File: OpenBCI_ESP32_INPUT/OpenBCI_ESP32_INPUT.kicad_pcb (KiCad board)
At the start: 2 copper layers, 50 x 50 mm, 75 parts, among them J1 Conn_02x13_Odd_Even, J2 Conn_02x08_Odd_Even, J3 Conn_02x03_Odd_Even, J4 Conn_02x02_Odd_Even, U1 TPD4E1B06, U2 TPD4E1B06, U3 TPD4E1B06, U4 TPD4E1B06, U5 TPD4E1B06, U6 TPD4E1B06, U7 ADS1299IPAG1

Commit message: Update Input Board Silk Screen
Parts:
- added R25: 0R, Resistor_SMD:R_0603_1608Metric, F.Cu at (124.6, 61.7)
- added R26: 0R, Resistor_SMD:R_0603_1608Metric, F.Cu at (119.8, 60.0)
- added R27: 0R, Resistor_SMD:R_0603_1608Metric, F.Cu at (124.6, 60.0)
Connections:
- C24 pad 2: /ADS1299/IBIAS -> Net-(C24-Pad2)
- R17 pad 2: /ADS1299/IBIAS -> Net-(C24-Pad2)
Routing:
- net Net-(C24-Pad2): track 0.00 -> 7.94 mm
- net Net-(C24-Pad1): track 8.88 -> 10.6 mm
- net /ADS1299/BIAS_INV: track 21.9 -> 22.9 mm

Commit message: Latest PCB file and firmware
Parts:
- added R28: 0R, Resistor_SMD:R_0603_1608Metric, F.Cu at (144.2, 63.8)
- added R29: 0R, Resistor_SMD:R_0603_1608Metric, F.Cu at (144.2, 65.5)
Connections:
- J2 pad 13: Net-(J2-Pad13) -> unconnected-(J2-Pad13)
- J2 pad 5: Net-(J2-Pad5) -> unconnected-(J2-Pad5)
- J2 pad 7: Net-(J2-Pad7) -> unconnected-(J2-Pad7)
- U1 pad 4: Net-(U1-Pad4) -> unconnected-(U1-Pad4)
- U6 pad 4: Net-(U6-Pad4) -> unconnected-(U6-Pad4)
- U6 pad 5: Net-(U6-Pad5) -> unconnected-(U6-Pad5)
- U7 pad 27: Net-(U7-Pad27) -> unconnected-(U7-Pad27)
- U7 pad 29: Net-(U7-Pad29) -> unconnected-(U7-Pad29)
- U7 pad 38: Net-(U7-Pad38) -> unconnected-(U7-Pad38)
- U7 pad 42: Net-(U7-Pad42) -> unconnected-(U7-Pad42)
- U7 pad 44: Net-(U7-Pad44) -> unconnected-(U7-Pad44)
- U7 pad 45: Net-(U7-Pad45) -> unconnected-(U7-Pad45)
- U7 pad 46: Net-(U7-Pad46) -> unconnected-(U7-Pad46)
- U7 pad 52: +3V3 -> Net-(U7-Pad52)
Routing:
- net Net-(U7-Pad52): track 0.00 -> 17.5 mm, vias 0 -> 2
- net GND: track 51.7 -> 56.1 mm
- net +2V5: track 75.7 -> 73.2 mm, vias 4 -> 3
- net -2V5: track 103.9 -> 102.6 mm
- net /ADS1299/CS: track 8.00 -> 7.19 mm
- added copper zone on F.Cu, net GND
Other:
- net class Default removed

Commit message: Code and STL updates
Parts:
- R28: value 0R -> NF
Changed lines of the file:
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@@
   (net 31 "unconnected-(J2-Pad7)")
   (net 32 "unconnected-(J2-Pad13)")
-  (net 33 "Net-(U7-Pad52)")
+  (net 33 "Net-(R28-Pad2)")
   (net 34 "unconnected-(U1-Pad4)")
   (net 35 "unconnected-(U6-Pad4)")
@@
       (net 2 "-2V5") (pinfunction "AVSS") (pintype "power_in"))
     (pad "21" smd roundrect locked (at -1.75 5.6625) (size 0.3 1.475) (layers "F.Cu" "F.Paste" "F.Mask") (roundrect_rratio 0.25)
-      (net 10 "+2V5") (pinfunction "AVDD") (pintype "passive"))
+      (net 10 "+2V5") (pinfunction "AVDD") (pintype "power_in"))
     (pad "22" smd roundrect locked (at -1.25 5.6625) (size 0.3 1.475) (layers "F.Cu" "F.Paste" "F.Mask") (roundrect_rratio 0.25)
-      (net 10 "+2V5") (pinfunction "AVDD") (pintype "passive"))
+      (net 10 "+2V5") (pinfunction "AVDD") (pintype "power_in"))
     (pad "23" smd roundrect locked (at -0.75 5.6625) (size 0.3 1.475) (layers "F.Cu" "F.Paste" "F.Mask") (roundrect_rratio 0.25)
-      (net 2 "-2V5") (pinfunction "AVSS") (pintype "passive"))
+      (net 2 "-2V5") (pinfunction "AVSS") (pintype "power_in"))
     (pad "24" smd roundrect locked (at -0.25 5.6625) (size 0.3 1.475) (layers "F.Cu" "F.Paste" "F.Mask") (roundrect_rratio 0.25)
       (net 7 "/ADS1299/VREF") (pinfunction "VREFP") (pintype "passive"))
@@
       (net 1 "GND") (pinfunction "RESV1") (pintype "input"))
     (pad "32" smd roundrect locked (at 3.75 5.6625) (size 0.3 1.475) (layers "F.Cu" "F.Paste" "F.Mask") (roundrect_rratio 0.25)
-      (net 2 "-2V5") (pinfunction "AVSS") (pintype "passive"))
+      (net 2 "-2V5") (pinfunction "AVSS") (pintype "power_in"))
     (pad "33" smd roundrect locked (at 5.6625 3.75) (size 1.475 0.3) (layers "F.Cu" "F.Paste" "F.Mask") (roundrect_rratio 0.25)
       (net 1 "GND") (pinfunction "DGND") (pintype "power_in"))
@@
       (net 9 "+3V3") (pinfunction "DVDD") (pintype "power_in"))
     (pad "49" smd roundrect locked (at 3.75 -5.6625) (size 0.3 1.475) (layers "F.Cu" "F.Paste" "F.Mask") (roundrect_rratio 0.25)
-      (net 1 "GND") (pinfunction "DGND") (pintype "passive"))
+      (net 1 "GND") (pinfunction "DGND") (pintype "power_in"))
     (pad "50" smd roundrect locked (at 3.25 -5.6625) (size 0.3 1.475) (layers "F.Cu" "F.Paste" "F.Mask") (roundrect_rratio 0.25)
-      (net 9 "+3V3") (pinfunction "DVDD") (pintype "passive"))
+      (net 9 "+3V3") (pinfunction "DVDD") (pintype "power_in"))
     (pad "51" smd roundrect locked (at 2.75 -5.6625) (size 0.3 1.475) (layers "F.Cu" "F.Paste" "F.Mask") (roundrect_rratio 0.25)
-      (net 1 "GND") (pinfunction "DGND") (pintype "passive"))
+      (net 1 "GND") (pinfunction "DGND") (pintype "power_in"))
     (pad "52" smd roundrect locked (at 2.25 -5.6625) (size 0.3 1.475) (layers "F.Cu" "F.Paste" "F.Mask") (roundrect_rratio 0.25)
-      (net 33 "Net-(U7-Pad52)") (pinfunction "CLKSEL") (pintype "input"))
+      (net 33 "Net-(R28-Pad2)") (pinfunction "CLKSEL") (pintype "input"))
     (pad "53" smd roundrect locked (at 1.75 -5.6625) (size 0.3 1.475) (layers "F.Cu" "F.Paste" "F.Mask") (roundrect_rratio 0.25)
       (net 2 "-2V5") (pinfunction "AVSS1") (pintype "power_in"))
@@
       (net 5 "Net-(C19-Pad1)") (pinfunction "VCAP3") (pintype "passive"))
     (pad "56" smd roundrect locked (at 0.25 -5.6625) (size 0.3 1.475) (layers "F.Cu" "F.Paste" "F.Mask") (roundrect_rratio 0.25)
-      (net 10 "+2V5") (pinfunction "AVDD") (pintype "passive"))
+      (net 10 "+2V5") (pinfunction "AVDD") (pintype "power_in"))
     (pad "57" smd roundrect locked (at -0.25 -5.6625) (size 0.3 1.475) (layers "F.Cu" "F.Paste" "F.Mask") (roundrect_rratio 0.25)
-      (net 2 "-2V5") (pinfunction "AVSS") (pintype "passive"))
+      (net 2 "-2V5") (pinfunction "AVSS") (pintype "power_in"))
     (pad "58" smd roundrect locked (at -0.75 -5.6625) (size 0.3 1.475) (layers "F.Cu" "F.Paste" "F.Mask") (roundrect_rratio 0.25)
-      (net 2 "-2V5") (pinfunction "AVSS") (pintype "passive"))
+      (net 2 "-2V5") (pinfunction "AVSS") (pintype "power_in"))
     (pad "59" smd roundrect locked (at -1.25 -5.6625) (size 0.3 1.475) (layers "F.Cu" "F.Paste" "F.Mask") (roundrect_rratio 0.25)
-      (net 10 "+2V5") (pinfunction "AVDD") (pintype "passive"))
+      (net 10 "+2V5") (pinfunction "AVDD") (pintype "power_in"))
     (pad "60" smd roundrect locked (at -1.75 -5.6625) (size 0.3 1.475) (layers "F.Cu" "F.Paste" "F.Mask") (roundrect_rratio 0.25)
       (net 1 "GND") (pinfunction "BIASREF") (pintype "input"))
@@
       (net 8 "Net-(C24-Pad1)") (pinfunction "BIASOUT") (pintype "output"))
     (pad "64" smd roundrect locked (at -3.75 -5.6625) (size 0.3 1.475) (layers "F.Cu" "F.Paste" "F.Mask") (roundrect_rratio 0.25)
-      (net 1 "GND") (pinfunction "RSRVD") (pintype "output"))
+      (net 1 "GND") (pinfunction "RSRVD") (pintype "input"))
     (model "${KICAD6_3DMODEL_DIR}/Package_QFP.3dshapes/TQFP-64_10x10mm_P0.5mm.wrl"
       (offset (xyz 0 0 0))
@@
     (fp_line (start -0.8 0.4125) (end -0.8 -0.4125) (layer "F.Fab") (width 0.1))
     (pad "1" smd roundrect locked (at -0.825 0) (size 0.8 0.95) (layers "F.Cu" "F.Paste" "F.Mask") (roundrect_rratio 0.25)
-      (net 33 "Net-(U7-Pad52)") (pintype "passive"))
+      (net 33 "Net-(R28-Pad2)") (pintype "passive"))
     (pad "2" smd roundrect locked (at 0.825 0) (size 0.8 0.95) (layers "F.Cu" "F.Paste" "F.Mask") (roundrect_rratio 0.25)
       (net 9 "+3V3") (pintype "passive"))
@@
       (effects (font (size 0.8 0.8) (thickness 0.1)))
     )
-    (fp_text value "0R" (at 0 1.43) (layer "F.Fab")
+    (fp_text value "NF" (at 0 1.43) (layer "F.Fab")
       (effects (font (size 1 1) (thickness 0.15)))
     )
@@
       (net 1 "GND") (pintype "passive"))
     (pad "2" smd roundrect locked (at 0.825 0) (size 0.8 0.95) (layers "F.Cu" "F.Paste" "F.Mask") (roundrect_rratio 0.25)
-      (net 33 "Net-(U7-Pad52)") (pintype "passive"))
+      (net 33 "Net-(R28-Pad2)") (pintype "passive"))
     (model "${KICAD6_3DMODEL_DIR}/Resistor_SMD.3dshapes/R_0603_1608Metric.wrl" hide
       (offset (xyz 0 0 0))

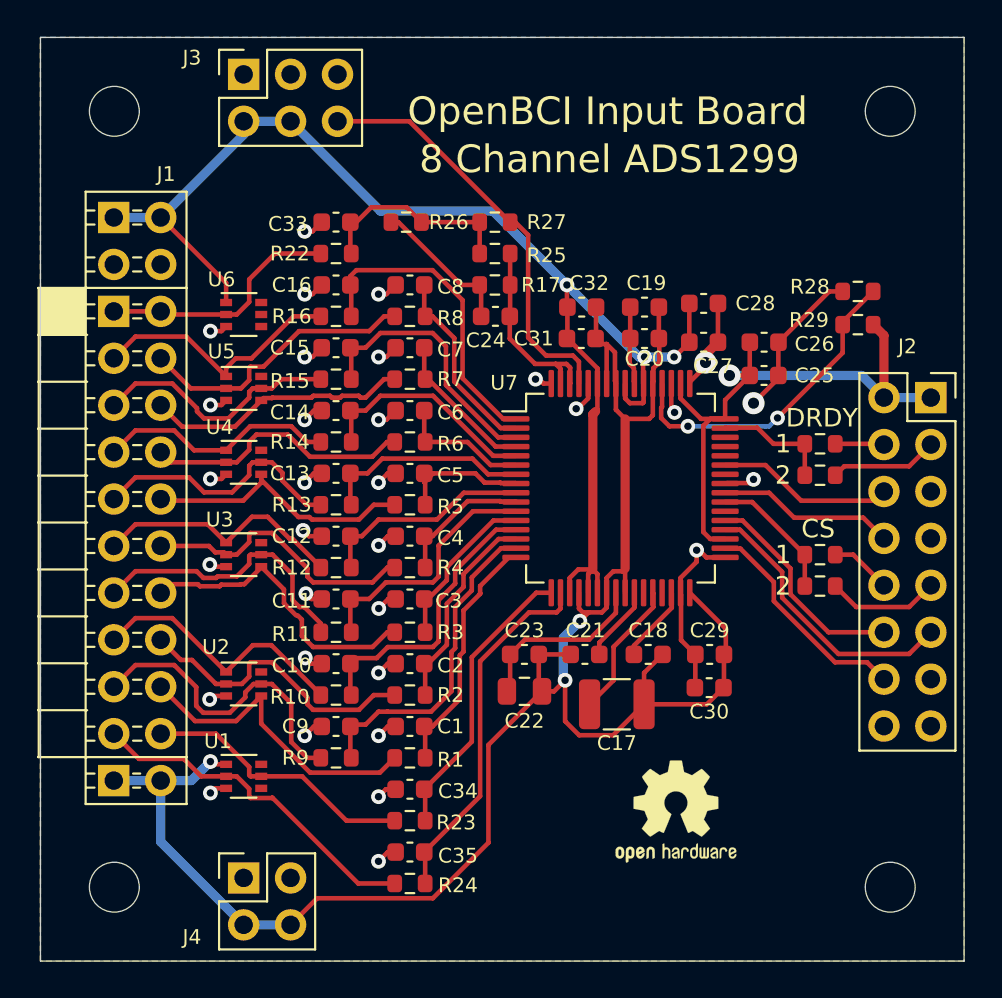
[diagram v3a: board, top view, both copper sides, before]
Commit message: add ADS1298 files
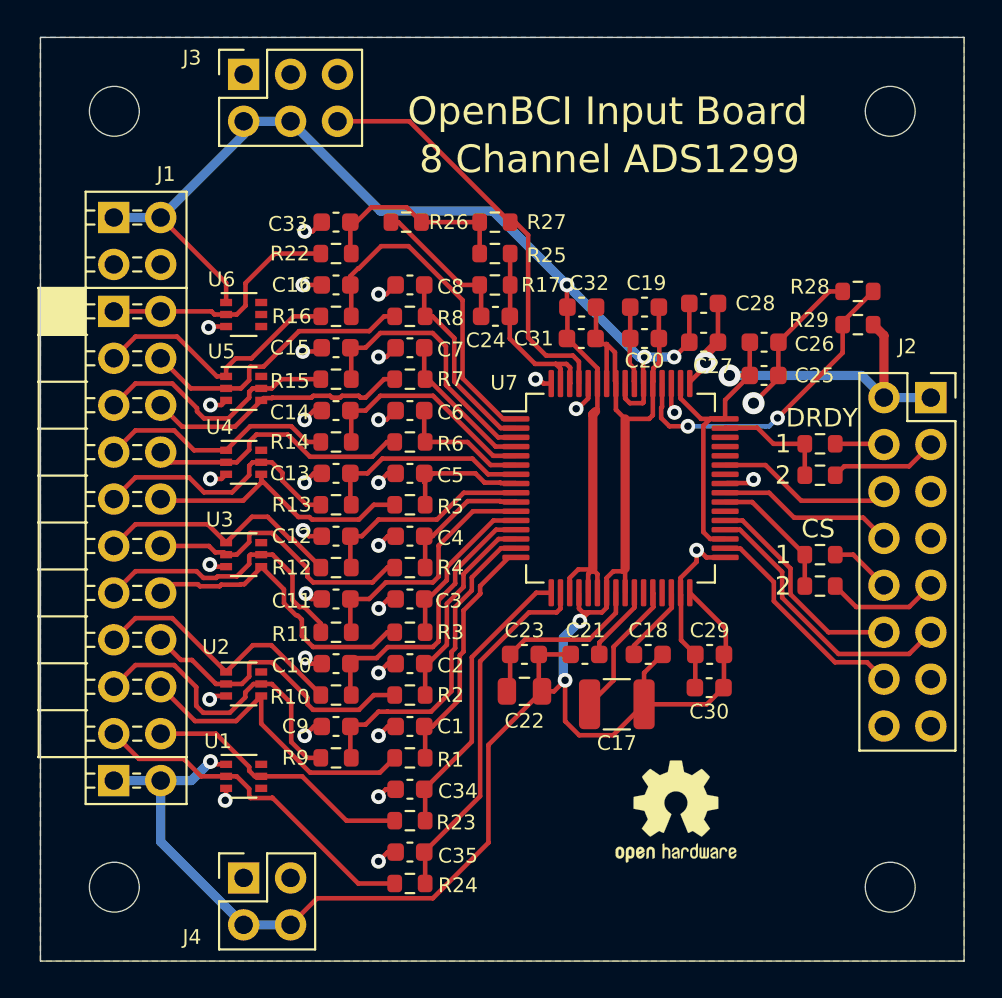
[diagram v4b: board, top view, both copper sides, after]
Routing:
- net /ADS1299/IN8N: track 17.1 -> 18.2 mm

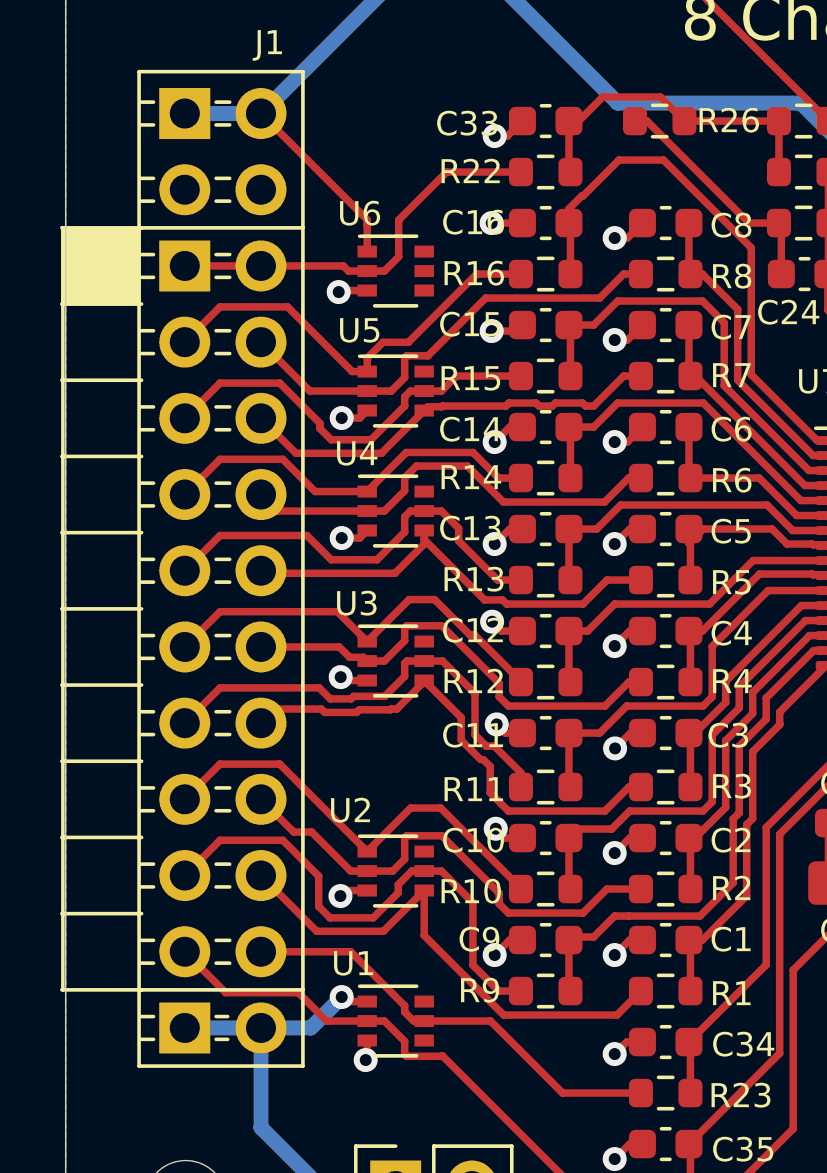
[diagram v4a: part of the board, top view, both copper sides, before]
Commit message: Update footprints
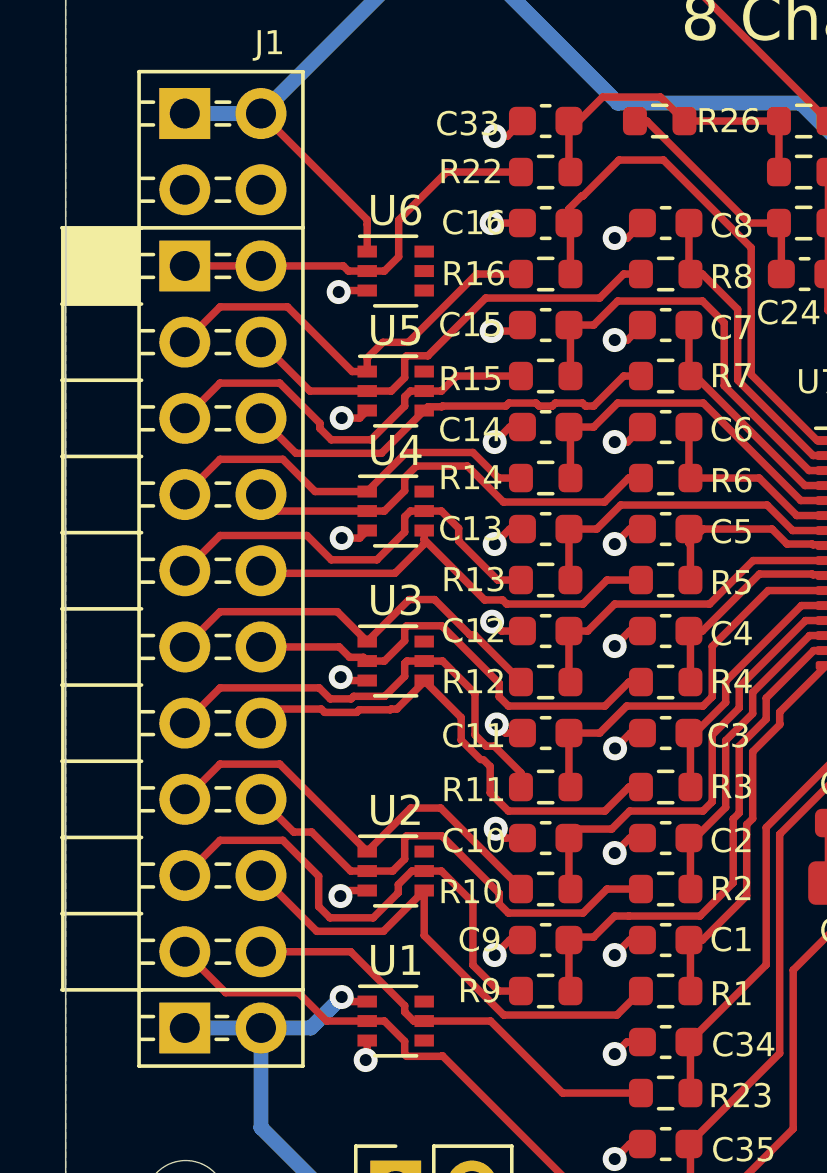
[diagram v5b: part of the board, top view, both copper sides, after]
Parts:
- C25, C27, C29, C31: value 1u -> 0.1u
- C26, C28, C30, C32: value 0.1u -> 1u
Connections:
- net +3V3 renamed +3.3V
- net /ADS1299/VREF renamed Net-(U7-VREFP)
